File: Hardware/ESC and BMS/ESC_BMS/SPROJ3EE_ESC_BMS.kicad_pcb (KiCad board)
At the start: 4 copper layers, 100 x 40 mm, 102 parts, among them J301 SW IN, J302 SW OUT, J401 1mm2_connector, J402 1mm2_connector, J403 1mm2_connector, J404 JST_8PH_2mm, J405 JST_3PH_2mm, J406 1mm2_connector, J407 1mm2_connector, J408 1mm2_connector, J409 1mm2_connector, J410 Barrel_Jack_Switch, Q201 SiR696DP, Q202 SiR696DP, Q203 SiR696DP, Q204 SiR696DP, Q205 SiR696DP, Q206 SiR696DP, Q301 SQJ141ELP, Q302 SQJ141ELP, Q303 FDV304P, Q304 PMV20XNEA, Q305 SQJ141ELP, U201 74AUC2G08, U202 74AUC2G08, U203 SN74LVC1G00DBV, U204 SN74LVC1G00DBV, U205 IR2301, U206 IR2301, U207 74AUC2G08, U208 SN74LVC1G00DBV, U209 TL331, U210 IR2301, U301 BQ2057W, U302 BQ2969

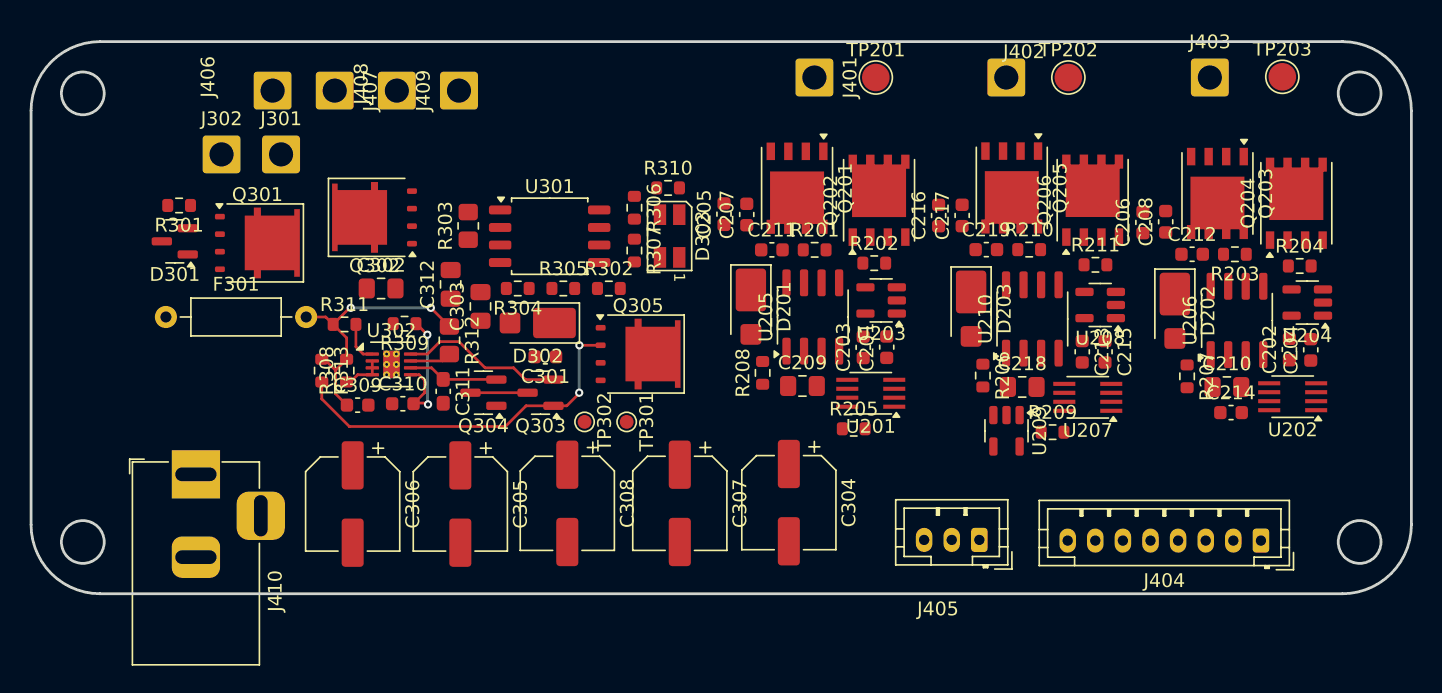
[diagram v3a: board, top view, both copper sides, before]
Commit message: ESC done
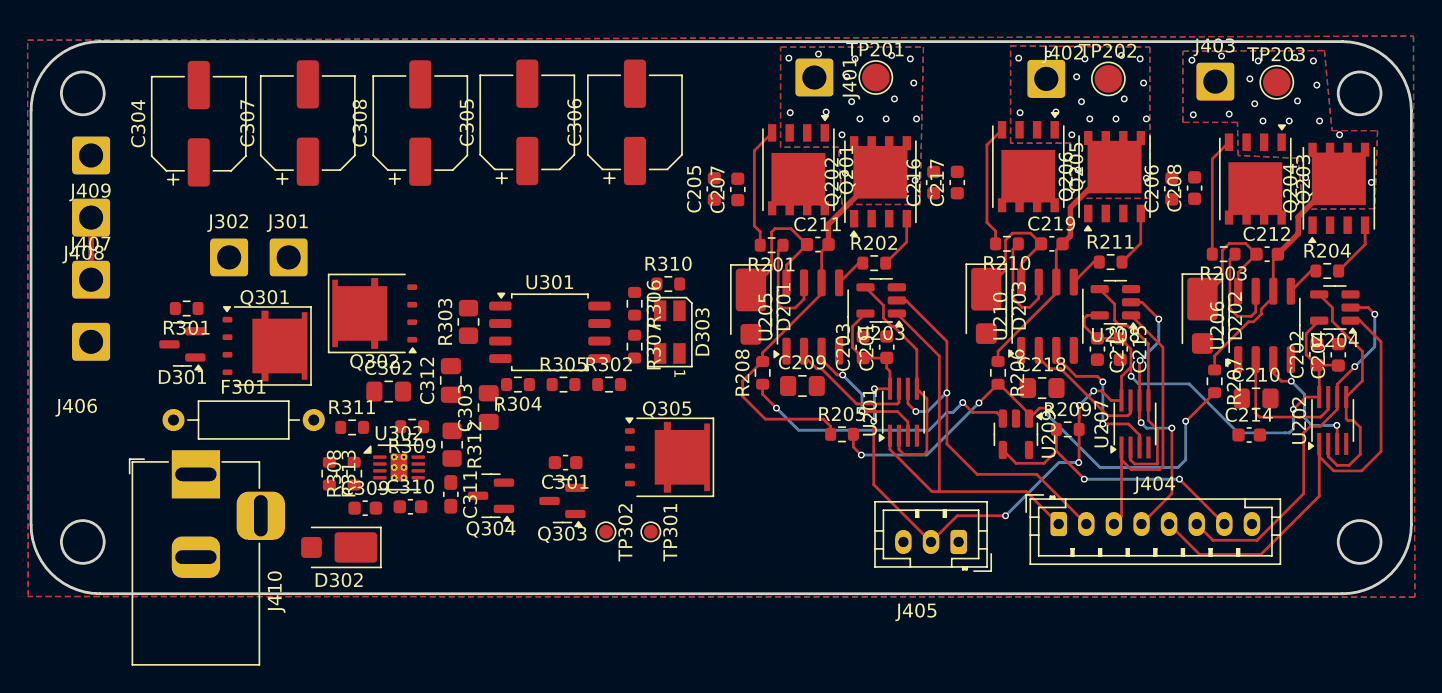
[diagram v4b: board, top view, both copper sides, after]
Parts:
- moved C304 50.8 mm to (107.2, 76.2), turned to 90 degrees
- moved C307 38.5 mm to (115.0, 76.2), turned to 90 degrees
- moved C306 34.4 mm to (138.8, 76.2), turned to 90 degrees
- moved C308 29.5 mm to (123.2, 76.2), turned to 90 degrees
- moved C305 28.1 mm to (130.9, 76.2), turned to 90 degrees
- moved J409 27.1 mm to (99.3, 78.5), turned to 180 degrees
- moved J408 24.0 mm to (99.3, 83.0), turned to 180 degrees
- moved J406 22.5 mm to (99.3, 92.0), turned to 180 degrees
- moved J407 22.3 mm to (99.3, 87.5), turned to 0 degrees
- moved D302 21.7 mm to (117.3, 106.9)
- moved J404 14.7 mm to (169.4, 105.2), turned to 0 degrees
- moved TP301 8.15 mm to (139.9, 105.8)
- moved TP302 8.11 mm to (136.7, 105.8)
- moved Q303 8.00 mm to (133.5, 103.6)
- moved C301 7.80 mm to (133.7, 100.8)
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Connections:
- C309 pad 1: Net-(Q305-D) -> Net-(Q305-S)
- C312 pad 1: +VCHARGE -> Net-(D302-K)
- D302 pad 1: GND -> Net-(D302-K)
- D302 pad 2: +VCHARGE -> /2. BMS/+VCHARGE
- F301 pad 2: Net-(Q305-D) -> Net-(Q305-S)
- J407 pad 1: /3. Connectors/VMID -> /2. BMS/VMID
- J408 pad 1: /3. Connectors/VMID -> /2. BMS/VMID
- J410 pad 1: +VCHARGE -> /2. BMS/+VCHARGE
- Q305 pad 1: Net-(Q305-D) -> +VPROT
- Q305 pad 3: +VPROT -> Net-(Q305-S)
- R302 pad 2: GND -> Net-(D302-K)
- R303 pad 1: GND -> Net-(D302-K)
- R305 pad 1: +VCHARGE -> /2. BMS/+VCHARGE
- R306 pad 1: GND -> Net-(D302-K)
- R308 pad 2: Net-(Q305-D) -> Net-(Q305-S)
- R311 pad 1: Net-(Q305-D) -> Net-(Q305-S)
- R312 pad 1: Net-(Q305-D) -> Net-(Q305-S)
- R313 pad 1: Net-(Q305-D) -> Net-(Q305-S)
- U301 pad 3: GND -> Net-(D302-K)
- U301 pad 8: GND -> Net-(D302-K)
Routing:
- net +3.3V: track 0.00 -> 78.7 mm, vias 0 -> 8
- net Net-(U209--): track 0.00 -> 37.0 mm, vias 0 -> 4
- net /1. ESC/CHS: track 0.00 -> 34.5 mm
- net /1. ESC/AHS: track 0.00 -> 29.7 mm
- net /1. ESC/ALS: track 0.00 -> 29.5 mm, vias 0 -> 2
- net A_PHASE: track 0.00 -> 28.2 mm, vias 0 -> 17
- net /1. ESC/CLS: track 0.00 -> 27.2 mm, vias 0 -> 2
- net Net-(Q303-D): track 26.7 -> 0.00 mm, vias 2 -> 0
- net /1. ESC/BHS: track 0.00 -> 22.0 mm
- net /1. ESC/BLS: track 0.00 -> 20.9 mm, vias 0 -> 4
- net /1. ESC/BEMF: track 0.00 -> 20.6 mm, vias 0 -> 2
- net Net-(U209-+): track 0.00 -> 20.5 mm, vias 0 -> 2
- net Net-(Q305-D): track 19.9 -> 0.00 mm, vias 2 -> 0
- net C_PHASE: track 0.00 -> 18.2 mm, vias 0 -> 17
- net /1. ESC/CNAND: track 0.00 -> 17.8 mm
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- added copper zone on B.Cu, net A_PHASE
- added copper zone on F.Cu, net A_PHASE
- added copper zone on In1.Cu, net A_PHASE
- added copper zone on In2.Cu, net A_PHASE
- added copper zone on B.Cu, net B_PHASE
- added copper zone on F.Cu, net B_PHASE
- added copper zone on In1.Cu, net B_PHASE
- added copper zone on In2.Cu, net B_PHASE
- added copper zone on B.Cu, net C_PHASE
- added copper zone on F.Cu, net C_PHASE
- added copper zone on In1.Cu, net C_PHASE
- added copper zone on In2.Cu, net C_PHASE
- added copper zone on B.Cu, net GND
- added copper zone on F.Cu, net GND

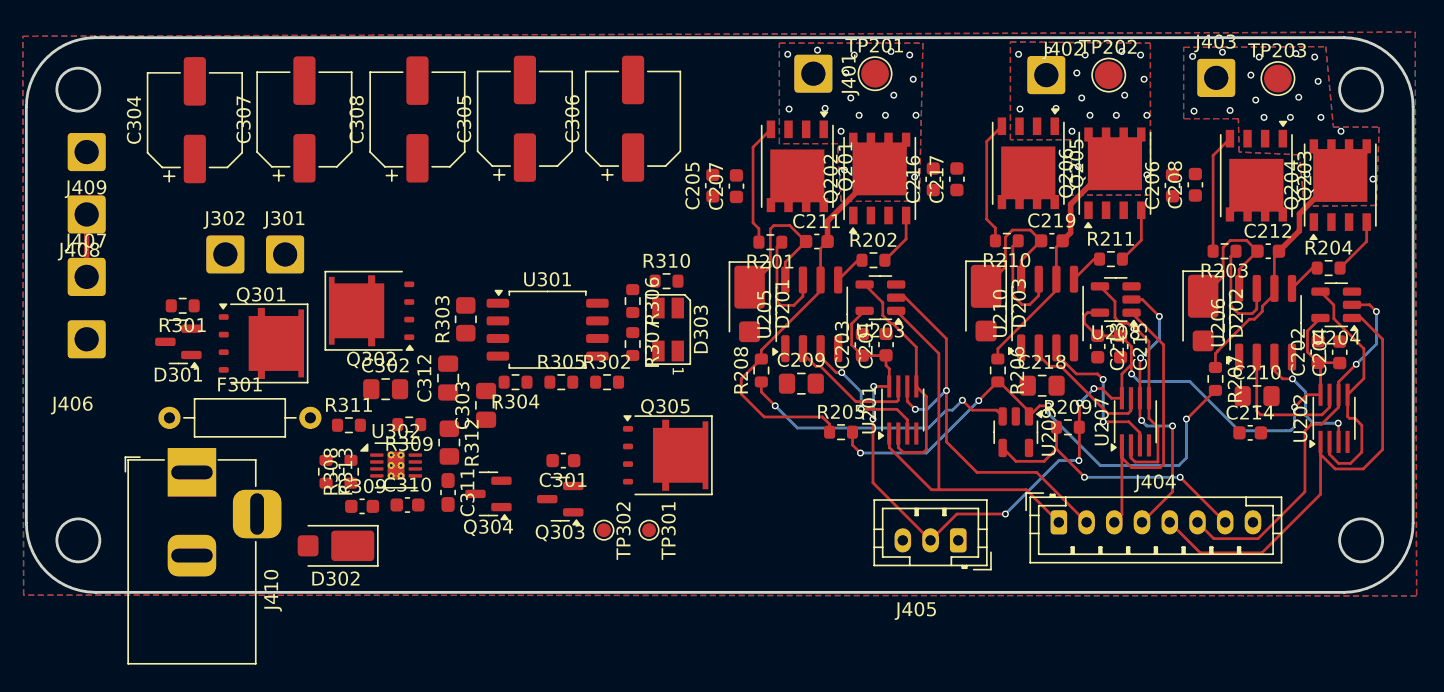
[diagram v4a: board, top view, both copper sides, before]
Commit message: ESC/BMS board done _/\_ (without silkscreen)
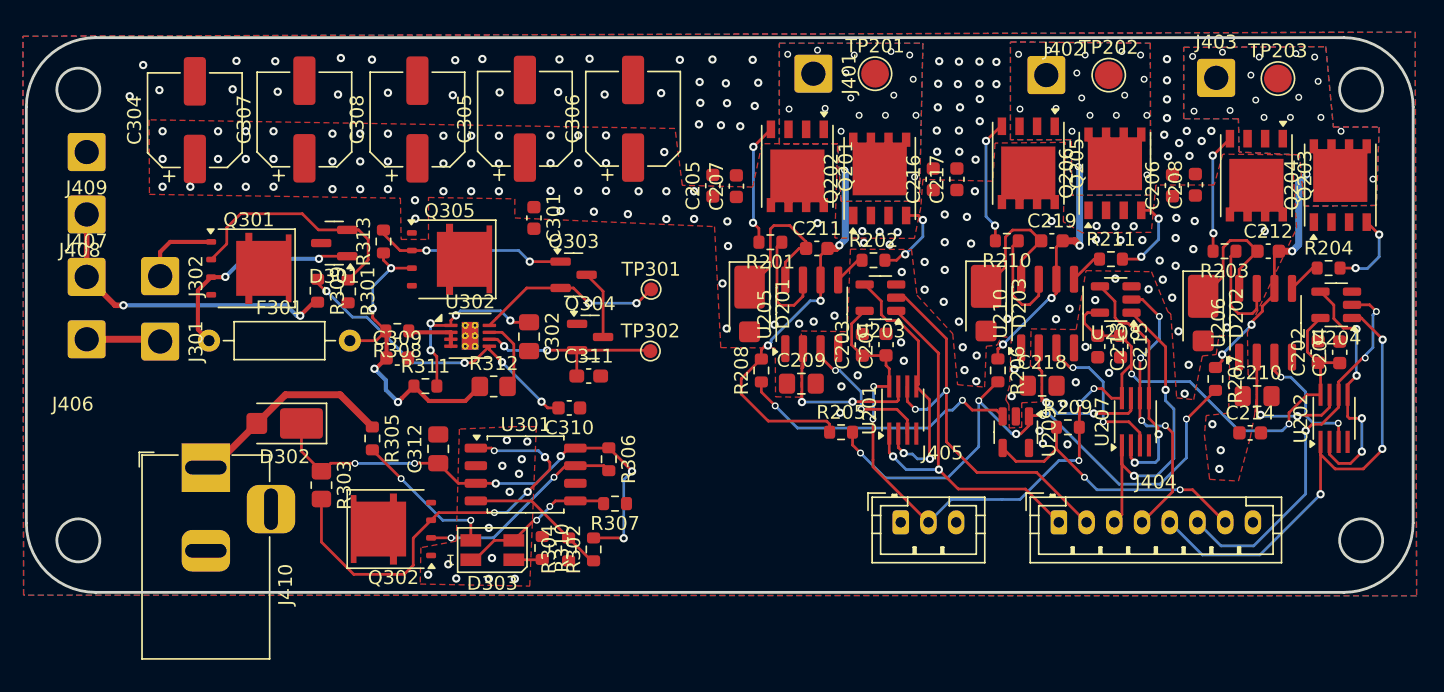
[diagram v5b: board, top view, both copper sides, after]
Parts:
- removed C303: 100n, Capacitor_SMD:C_0805_2012Metric_Pad1.18x1.45mm_HandSolder
- moved R310 21.2 mm to (132.2, 107.1), turned to -90 degrees
- moved Q305 21.0 mm to (125.5, 86.3)
- moved D303 20.3 mm to (128.6, 107.2), turned to 180 degrees
- moved C301 17.6 mm to (131.6, 83.3), turned to -90 degrees
- moved TP301 17.4 mm to (140.1, 88.5), turned to 0 degrees
- moved R313 17.1 mm to (120.8, 85.0), turned to 90 degrees
- moved Q303 16.2 mm to (134.5, 87.4), turned to 0 degrees
- moved R303 15.9 mm to (116.3, 102.6), turned to -90 degrees
- moved Q302 15.8 mm to (121.5, 105.7)
- moved R305 14.2 mm to (120.0, 99.2), turned to -90 degrees
- moved C310 13.6 mm to (134.2, 97.0), turned to 180 degrees
- moved Q304 13.5 mm to (135.7, 91.9), turned to 0 degrees
- moved TP302 13.3 mm to (140.0, 92.9), turned to 0 degrees
- moved D301 13.3 mm to (117.2, 85.1)
- moved C311 13.2 mm to (135.6, 94.7), turned to 0 degrees
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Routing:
- net Net-(D302-K): track 0.00 -> 36.5 mm, vias 0 -> 6
- net Net-(Q302-S): track 0.00 -> 31.2 mm, vias 0 -> 4
- net Net-(Q305-S): track 0.00 -> 24.8 mm, vias 0 -> 4
- net Net-(U302-V1): track 0.00 -> 22.5 mm, vias 0 -> 4
- net /2. BMS/VMID: track 4.50 -> 22.7 mm, vias 0 -> 2
- net Net-(D301-A): track 0.00 -> 17.7 mm
- net Net-(D301-K): track 0.00 -> 15.7 mm, vias 0 -> 2
- net Net-(Q302-G): track 0.00 -> 15.2 mm, vias 0 -> 2
- net /2. BMS/+VCHARGE: track 0.00 -> 15.1 mm
- net Net-(Q303-D): track 0.00 -> 14.2 mm, vias 0 -> 2
- net Net-(Q304-G): track 0.00 -> 13.9 mm, vias 0 -> 2
- net Net-(Q303-G): track 0.00 -> 13.8 mm, vias 0 -> 2
- net VDD: track 0.00 -> 13.0 mm, vias 0 -> 4
- net Net-(D303-A1): track 0.00 -> 11.4 mm, vias 0 -> 2
- net Net-(D303-A2): track 0.00 -> 10.7 mm, vias 0 -> 2
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- added copper zone on F.Cu, net +VPROT

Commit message: ESC/BMS board done _/\_ (with full silkscreen) - just 12 warnings
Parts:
- moved R310 0.32 mm to (132.5, 107.2)
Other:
- board text added: "A PHASE"
- board text added: "B PHASE"
- board text added: "C PHASE"
- board text added: "OUT"
- board text added: "REG"

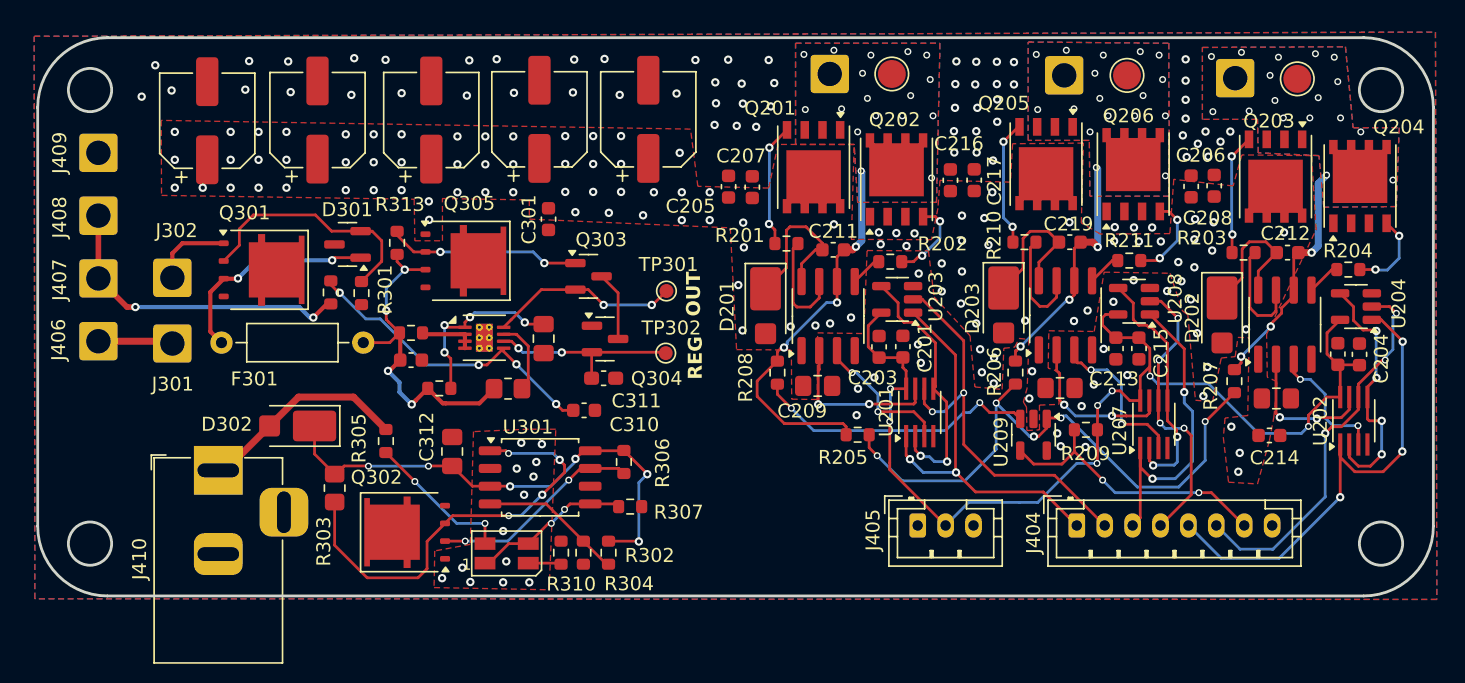
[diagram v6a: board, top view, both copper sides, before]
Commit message: Light rework of ESC/BMS layout
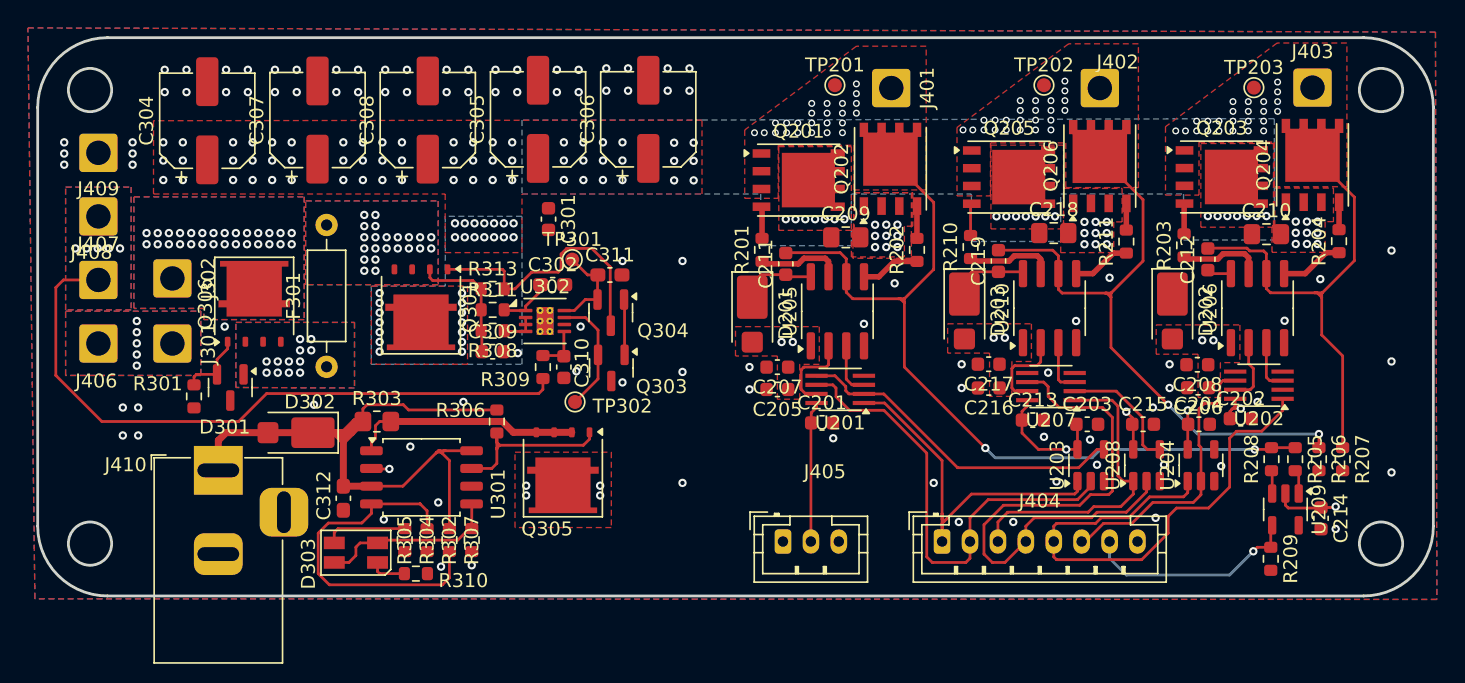
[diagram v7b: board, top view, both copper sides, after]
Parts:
- removed Q302: SQJ141ELP, Package_SO:PowerPAK_SO-8L_Single
- removed R312: 1M, Resistor_SMD:R_0805_2012Metric_Pad1.20x1.40mm_HandSolder
- added Q306: SQJQ131EL, Package_SO:PowerPAK_SO-8L_Single, F.Cu at (110.5, 89.4)
- C302, C312: footprint Capacitor_SMD:C_0805_2012Metric_Pad1.18x1.45mm_HandSolder -> Capacitor_SMD:C_0603_1608Metric_Pad1.08x0.95mm_HandSolder
- Q301, Q305: value SQJ141ELP -> SQJQ131EL
- TP201, TP202, TP203: footprint TestPoint:TestPoint_Pad_D2.0mm -> TestPoint:TestPoint_Pad_D1.0mm
- moved R208 35.9 mm to (183.4, 100.5)
- moved R205 31.4 mm to (185.1, 100.5), turned to -90 degrees
- moved R206 22.6 mm to (186.8, 100.5)
- moved U209 18.8 mm to (184.4, 104.1)
- moved U203 18.3 mm to (170.4, 100.9), turned to 90 degrees
- moved Q305 16.6 mm to (132.6, 101.3), turned to -90 degrees
- moved R209 16.2 mm to (183.3, 107.6), turned to -90 degrees
- moved R309 16.1 mm to (131.2, 93.9)
- moved C203 15.9 mm to (170.2, 98.0), turned to 0 degrees
- moved U204 15.9 mm to (178.3, 100.9), turned to 90 degrees
- moved C216 15.1 mm to (163.1, 95.4), turned to 180 degrees
- moved C205 14.9 mm to (148.0, 95.5), turned to 180 degrees
- moved C206 14.4 mm to (178.1, 95.4), turned to 180 degrees
- moved R301 14.1 mm to (106.2, 96.0)
- moved D301 13.3 mm to (108.8, 95.4), turned to -90 degrees
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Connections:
- C309 pad 1: Net-(Q305-S) -> /2. BMS/Poly_OUT
- D301 pad 1: Net-(D301-K) -> /2. BMS/Poly_IN
- F301 pad 1: Net-(D301-K) -> /2. BMS/Poly_IN
- F301 pad 2: Net-(Q305-S) -> /2. BMS/Poly_OUT
- J302 pad 1: Net-(Q301-D) -> /2. BMS/SW_OUT
- Q301 pad 1: Net-(Q301-D) -> Net-(Q301-G)
- Q301 pad 2: Net-(D301-A) -> /2. BMS/Poly_OUT
- Q301 pad 3: Net-(D301-K) -> /2. BMS/Poly_OUT
- Q301 pad 4: (no net) -> /2. BMS/Poly_OUT
- Q301 pad 5: (no net) -> +VPROT
- Q303 pad 3: Net-(Q303-S) -> GND
- Q304 pad 1: GND -> Net-(Q303-D)
- Q304 pad 3: Net-(Q303-S) -> Net-(Q301-G)
- Q305 pad 1: +VPROT -> Net-(Q305-G)
- Q305 pad 2: Net-(Q303-D) -> Net-(U301-SNS)
- Q305 pad 3: Net-(Q305-S) -> Net-(U301-SNS)
- Q305 pad 4: (no net) -> Net-(U301-SNS)
- Q305 pad 5: (no net) -> +VPROT
- R303 pad 2: Net-(Q302-S) -> Net-(U301-SNS)
- R306 pad 2: Net-(Q302-G) -> Net-(Q305-G)
- R308 pad 2: Net-(Q305-S) -> /2. BMS/Poly_OUT
- R311 pad 1: Net-(Q305-S) -> /2. BMS/Poly_OUT
- R313 pad 1: Net-(Q305-S) -> /2. BMS/Poly_OUT
- R313 pad 2: Net-(Q303-D) -> Net-(Q301-G)
- TP301 pad 1: Net-(Q303-G) -> Net-(Q304-G)
- TP302 pad 1: Net-(Q304-G) -> Net-(Q303-G)
- U301 pad 1: Net-(Q302-S) -> Net-(U301-SNS)
- U301 pad 7: Net-(Q302-G) -> Net-(Q305-G)
- U302 pad 6: Net-(Q304-G) -> GND
- U302 pad 7: Net-(U302-CTL) -> Net-(Q303-G)
- U302 pad 8: Net-(Q303-G) -> Net-(Q304-G)
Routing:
- net Net-(U209--): track 43.3 -> 1.74 mm, vias 5 -> 0
- net Net-(Q302-S): track 31.2 -> 0.00 mm, vias 4 -> 0
- net A_PHASE: track 28.8 -> 59.8 mm, vias 20 -> 26
- net B_PHASE: track 18.0 -> 45.6 mm, vias 20 -> 26
- net /2. BMS/VMID: track 22.7 -> 47.6 mm, vias 2 -> 5
- net Net-(Q305-S): track 24.8 -> 0.00 mm, vias 4 -> 0
- net +3.3V: track 76.6 -> 99.7 mm, vias 7 -> 4
- net /1. ESC/BLS: track 20.6 -> 40.5 mm, vias 4 -> 0
- net Net-(Q301-G): track 0.00 -> 19.6 mm
- net Net-(U302-V1): track 22.5 -> 3.31 mm, vias 4 -> 0
- net Net-(U209-+): track 20.5 -> 1.66 mm, vias 2 -> 0
- net /1. ESC/CNAND: track 18.3 -> 0.00 mm, vias 4 -> 0
- net C_PHASE: track 17.7 -> 35.4 mm, vias 20 -> 24
- net Net-(U301-SNS): track 0.00 -> 16.4 mm
- net Net-(D301-K): track 15.7 -> 0.00 mm, vias 2 -> 0
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- added copper zone on B.Cu, net +VPROT
- added copper zone on B.Cu, net /2. BMS/+VBATT
- added copper zone on F.Cu, net /2. BMS/+VBATT
- added copper zone on B.Cu, net /2. BMS/Poly_IN
- added copper zone on F.Cu, net /2. BMS/Poly_IN
- added copper zone on B.Cu, net /2. BMS/Poly_OUT
- added copper zone on F.Cu, net /2. BMS/Poly_OUT
- added copper zone on B.Cu, net /2. BMS/SW_OUT
- added copper zone on F.Cu, net /2. BMS/SW_OUT
- added copper zone on B.Cu, net /2. BMS/VMID
- added copper zone on F.Cu, net /2. BMS/VMID
- removed copper zone on B.Cu, net A_PHASE
- removed copper zone on B.Cu, net B_PHASE
- removed copper zone on B.Cu, net C_PHASE
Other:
- board text removed: "A PHASE"
- board text removed: "B PHASE"
- board text removed: "C PHASE"
- board text removed: "OUT"
- board text removed: "REG"
